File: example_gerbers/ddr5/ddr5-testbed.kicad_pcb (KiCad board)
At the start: 6 copper layers, 18.5 x 20 mm, 42 parts, among them U1 MT60B2G8HB-48B_A

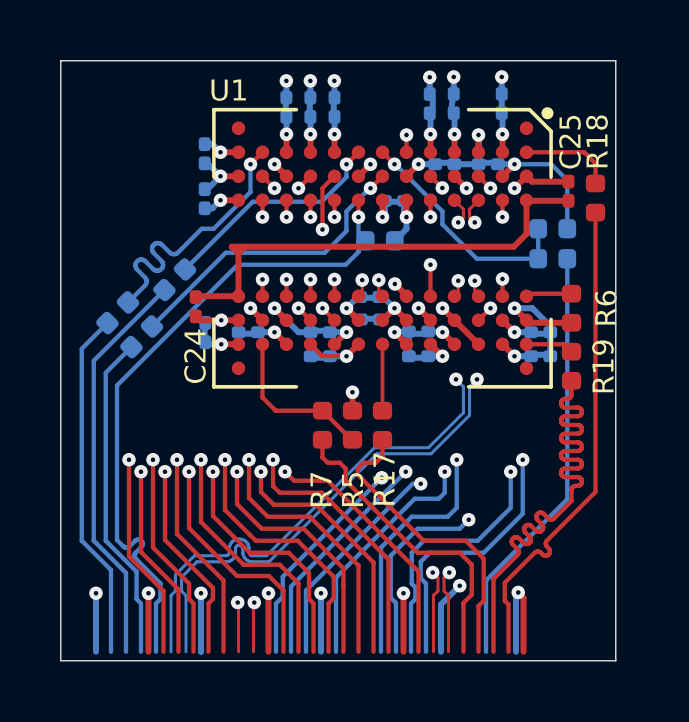
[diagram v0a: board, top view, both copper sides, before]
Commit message: More optimization for ddr5 example
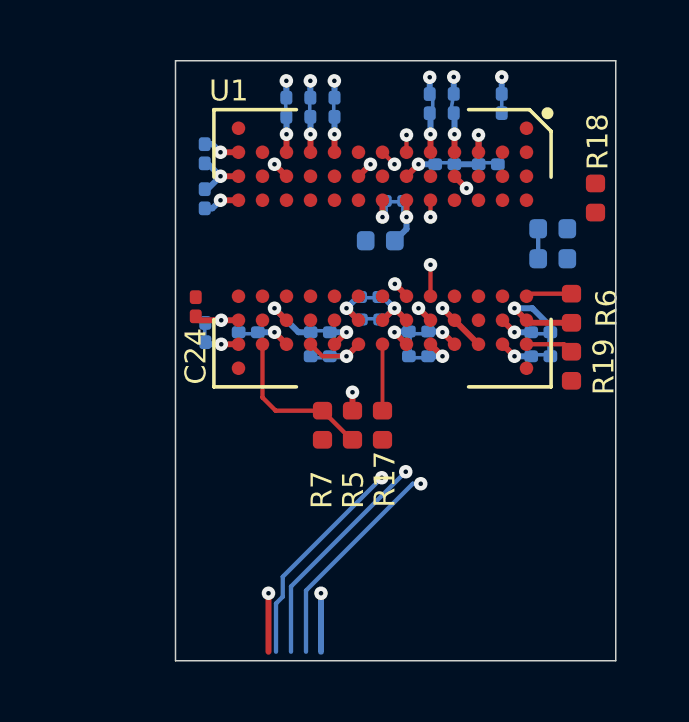
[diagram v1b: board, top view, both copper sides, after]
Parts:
- removed C25: C_100n_0201, ddr5-testbed-footprints:0201-res
- removed R15, R16, R4: R_0R_0402, ddr5-testbed-footprints:0402-res
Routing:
- net CS_N: track 22.3 -> 0.00 mm, vias 1 -> 0
- net CA8: track 22.1 -> 0.00 mm, vias 2 -> 0
- net CA10: track 22.1 -> 0.00 mm, vias 2 -> 0
- net CA6: track 22.0 -> 0.00 mm, vias 2 -> 0
- net CA2: track 22.0 -> 0.00 mm, vias 2 -> 0
- net CA5: track 22.0 -> 0.00 mm, vias 2 -> 0
- net CA11: track 22.0 -> 0.00 mm, vias 2 -> 0
- net CA9: track 22.0 -> 0.00 mm, vias 2 -> 0
- net CA7: track 22.0 -> 0.00 mm, vias 2 -> 0
- net CA3: track 22.0 -> 0.00 mm, vias 2 -> 0
- net CA4: track 22.0 -> 0.00 mm, vias 2 -> 0
- net CA1: track 22.0 -> 0.00 mm, vias 2 -> 0
- net CLK_P: track 22.0 -> 0.00 mm, vias 2 -> 0
- net CLK_N: track 22.0 -> 0.00 mm, vias 2 -> 0
- net CA0: track 22.0 -> 0.00 mm, vias 2 -> 0
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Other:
- board size 18.5 x 20 mm -> 14.7 x 20 mm
